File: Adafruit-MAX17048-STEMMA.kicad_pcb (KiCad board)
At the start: 2 copper layers, 25.4 x 20.3 mm, 24 parts, among them X1 JST 2 PH, X2 JST 2 PH, X3 MAX17048/T

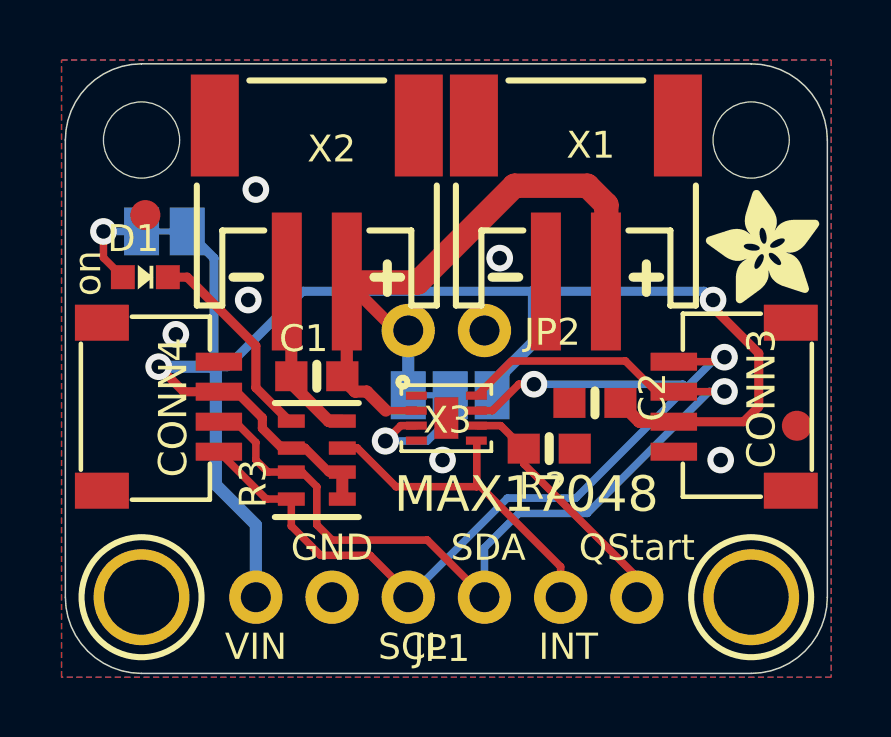
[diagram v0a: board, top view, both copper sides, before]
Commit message: Remove orphan N$4 copper stub inherited from upstream
In the Eagle source, signal N$4 has zero contactrefs and a single wire
segment: a 0.635 mm dangling stub on B.Cu that overlapped SJ2's VDD pad
and ran within 0.076 mm of the VBAT trace. It connected nothing, so the
board worked, but it was stray copper rather than intentional design.

Clears the shorting_items violation and two clearance violations, leaving
only the two SJ1 solder-jumper ones. DRC total 106 -> 96.

Co-Authored-By: Claude Opus 5 <noreply@anthropic.com>
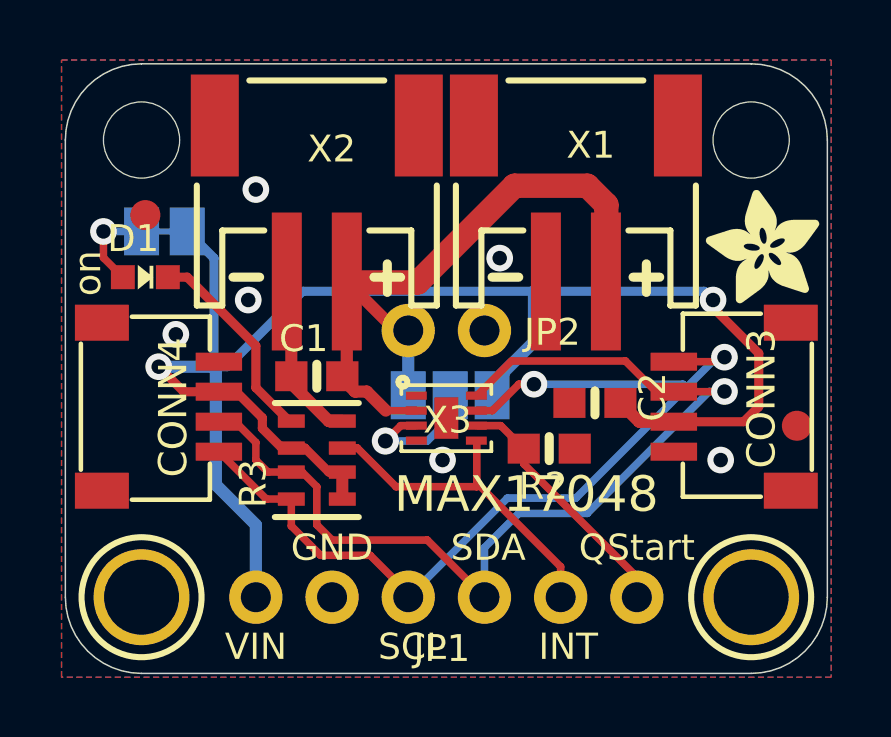
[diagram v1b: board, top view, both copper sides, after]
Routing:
- net N$4: track 0.63 -> 0.00 mm
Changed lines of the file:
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@@
 		(net "VDD")
-	)
-	(segment
-		(start 148.2471 105.8926)
-		(end 147.6121 105.8926)
-		(width 0.2032)
-		(layer "B.Cu")
-		(net "N$4")
 	)
 	(zone
